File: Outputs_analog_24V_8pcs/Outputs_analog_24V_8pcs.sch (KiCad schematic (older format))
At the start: 10 parts, among them J1 Screw_Terminal_01x02, J2 Screw_Terminal_01x02, J3 Screw_Terminal_01x06, U1 74HC595

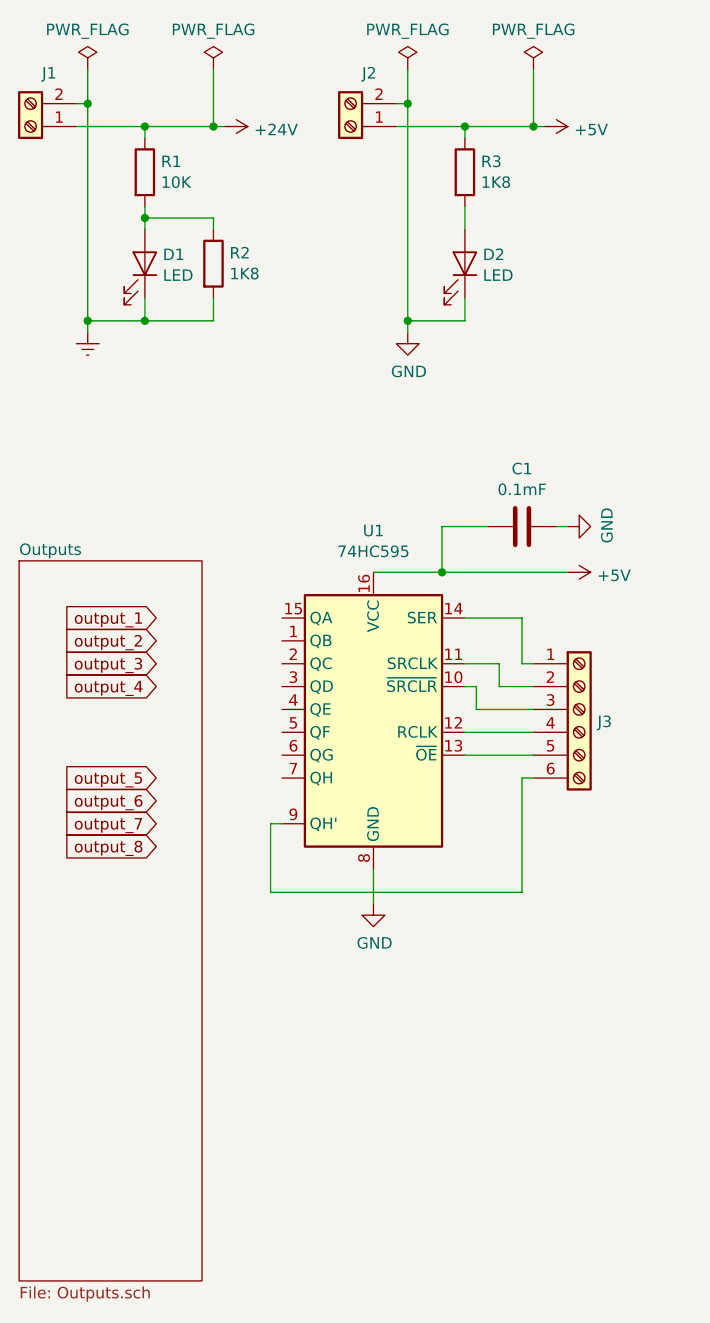
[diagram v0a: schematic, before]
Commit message: Update Outputs pcb
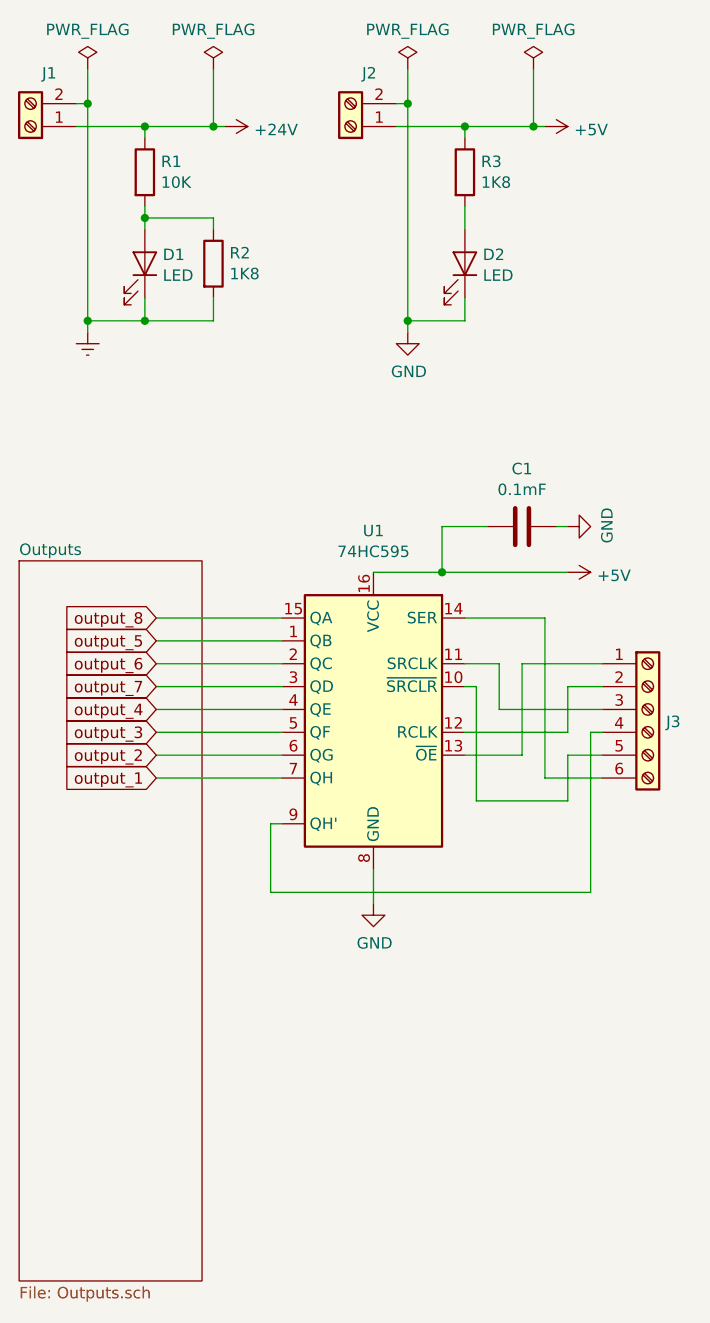
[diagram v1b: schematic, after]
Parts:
- D1, D2: footprint Diode_THT:D_A-405_P2.54mm_Vertical_AnodeUp -> LED_THT:LED_D3.0mm
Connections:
- net output_1: now also U1.7 (QH)
- net output_2: now also U1.6 (QG)
- net output_3: now also U1.5 (QF)
- net output_4: now also U1.4 (QE)
- net output_5: now also U1.1 (QB)
- net output_6: now also U1.2 (QC)
- net output_7: now also U1.3 (QD)
- net output_8: now also U1.15 (QA)
- net at J3.1 (Pin_1): now also U1.13 (~OE); no longer U1.14 (SER)
- net at J3.2 (Pin_2): now also U1.12 (RCLK); no longer U1.11 (SRCLK)
- net at J3.3 (Pin_3): now also U1.11 (SRCLK); no longer U1.10 (~SRCLR)
- net at J3.4 (Pin_4): now also U1.9 (QH'); no longer U1.12 (RCLK)
- net at J3.5 (Pin_5): now also U1.10 (~SRCLR); no longer U1.13 (~OE)
- net at J3.6 (Pin_6): now also U1.14 (SER); no longer U1.9 (QH')
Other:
- moved on the sheet: J3
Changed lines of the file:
@@
 EESchema Schematic File Version 4
-EELAYER 30 0
+LIBS:Outputs_analog_24V_8pcs-cache
+EELAYER 26 0
 EELAYER END
 $Descr A4 11693 8268
@@
 F 0 "D1" V 1589 2128 50  0000 L CNN
 F 1 "LED" V 1498 2128 50  0000 L CNN
-F 2 "Diode_THT:D_A-405_P2.54mm_Vertical_AnodeUp" H 1550 2050 50  0001 C CNN
+F 2 "LED_THT:LED_D3.0mm" H 1550 2050 50  0001 C CNN
 F 3 "~" H 1550 2050 50  0001 C CNN
 	1    1550 2050
@@
 F 0 "D2" V 2989 2128 50  0000 L CNN
 F 1 "LED" V 2898 2128 50  0000 L CNN
-F 2 "Diode_THT:D_A-405_P2.54mm_Vertical_AnodeUp" H 2950 2050 50  0001 C CNN
+F 2 "LED_THT:LED_D3.0mm" H 2950 2050 50  0001 C CNN
 F 3 "~" H 2950 2050 50  0001 C CNN
 	1    2950 2050
@@
 F1 "Outputs.sch" 50
 $EndSheet
+Text GLabel 1600 4300 0    50   Input ~ 0
+output_1
+Text GLabel 1600 4200 0    50   Input ~ 0
+output_2
+Text GLabel 1600 4100 0    50   Input ~ 0
+output_3
+Text GLabel 1600 4000 0    50   Input ~ 0
+output_4
+Text GLabel 1600 3700 0    50   Input ~ 0
+output_5
+Text GLabel 1600 3800 0    50   Input ~ 0
+output_6
+Text GLabel 1600 3900 0    50   Input ~ 0
+output_7
 Text GLabel 1600 3600 0    50   Input ~ 0
-output_1
-Text GLabel 1600 3700 0    50   Input ~ 0
-output_2
-Text GLabel 1600 3800 0    50   Input ~ 0
-output_3
-Text GLabel 1600 3900 0    50   Input ~ 0
-output_4
-Text GLabel 1600 4300 0    50   Input ~ 0
-output_5
-Text GLabel 1600 4400 0    50   Input ~ 0
-output_6
-Text GLabel 1600 4500 0    50   Input ~ 0
-output_7
-Text GLabel 1600 4600 0    50   Input ~ 0
 output_8
-$Comp
-L Connector:Screw_Terminal_01x06 J3
-U 1 1 5EADD649
-P 3450 4000
-F 0 "J3" H 3530 3946 50  0000 L CNN
-F 1 "Screw_Terminal_01x06" H 3530 3901 50  0001 L CNN
-F 2 "Connector_PinHeader_2.54mm:PinHeader_1x06_P2.54mm_Horizontal" H 3450 4000 50  0001 C CNN
-F 3 "~" H 3450 4000 50  0001 C CNN
-	1    3450 4000
-	1    0    0    -1
-$EndComp
 $Comp
 L 74xx:74HC595 U1
@@
 $EndComp
 Wire Wire Line
-	2950 3600 3200 3600
-Wire Wire Line
-	3200 3600 3200 3800
-Wire Wire Line
-	3200 3800 3250 3800
+	2150 4500 2100 4500
+Wire Wire Line
+	2100 4500 2100 4800
+Wire Wire Line
+	2550 4700 2550 4850
+Wire Wire Line
+	2850 3400 3400 3400
+Wire Wire Line
+	1600 4300 2150 4300
+Wire Wire Line
+	1600 4200 2150 4200
+Wire Wire Line
+	1600 4100 2150 4100
+Wire Wire Line
+	1600 4000 2150 4000
+Wire Wire Line
+	1600 3600 2150 3600
+Wire Wire Line
+	1600 3900 2150 3900
+Wire Wire Line
+	1600 3700 2150 3700
+Wire Wire Line
+	1600 3800 2150 3800
+$Comp
+L Connector:Screw_Terminal_01x06 J3
+U 1 1 5EADD649
+P 3750 4000
+F 0 "J3" H 3830 3946 50  0000 L CNN
+F 1 "Screw_Terminal_01x06" H 3830 3901 50  0001 L CNN
+F 2 "Connector_PinHeader_2.54mm:PinHeader_1x06_P2.54mm_Horizontal" H 3750 4000 50  0001 C CNN
+F 3 "~" H 3750 4000 50  0001 C CNN
+	1    3750 4000
+	1    0    0    -1
+$EndComp
+Wire Wire Line
+	2950 4100 3400 4100
+Wire Wire Line
+	3400 4100 3400 3900
+Wire Wire Line
+	3400 3900 3550 3900
+Wire Wire Line
+	3550 4100 3500 4100
+Wire Wire Line
+	3500 4100 3500 4800
+Wire Wire Line
+	3500 4800 2100 4800
+Wire Wire Line
+	3200 4200 3200 3800
+Wire Wire Line
+	3200 3800 3550 3800
+Wire Wire Line
+	2950 4200 3200 4200
+Wire Wire Line
+	2950 3600 3300 3600
+Wire Wire Line
+	3300 3600 3300 4300
+Wire Wire Line
+	3300 4300 3550 4300
 Wire Wire Line
 	2950 3800 3100 3800
 Wire Wire Line
-	3100 3800 3100 3900
-Wire Wire Line
-	3100 3900 3250 3900
+	3100 3800 3100 4000
+Wire Wire Line
+	3100 4000 3550 4000
 Wire Wire Line
 	2950 3900 3000 3900
 Wire Wire Line
-	3000 3900 3000 4000
-Wire Wire Line
-	3000 4000 3250 4000
-Wire Wire Line
-	2950 4100 3250 4100
-Wire Wire Line
-	2950 4200 3250 4200
-Wire Wire Line
-	2150 4500 2100 4500
-Wire Wire Line
-	2100 4500 2100 4800
-Wire Wire Line
-	2100 4800 3200 4800
-Wire Wire Line
-	3200 4800 3200 4300
-Wire Wire Line
-	3200 4300 3250 4300
-Wire Wire Line
-	2550 4700 2550 4850
-Wire Wire Line
-	2850 3400 3400 3400
+	3000 3900 3000 4400
+Wire Wire Line
+	3000 4400 3400 4400
+Wire Wire Line
+	3400 4400 3400 4200
+Wire Wire Line
+	3400 4200 3550 4200
 $EndSCHEMATC

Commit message: Update pcb
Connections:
- net output_2: now also U1.4 (QE); no longer U1.6 (QG)
- net output_4: now also U1.6 (QG); no longer U1.4 (QE)
- net output_5: now also U1.15 (QA); no longer U1.1 (QB)
- net output_6: now also U1.1 (QB); no longer U1.2 (QC)
- net output_8: now also U1.2 (QC); no longer U1.15 (QA)
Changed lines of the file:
@@
 EESchema Schematic File Version 4
-LIBS:Outputs_analog_24V_8pcs-cache
-EELAYER 26 0
+EELAYER 30 0
 EELAYER END
 $Descr A4 11693 8268
@@
 Text GLabel 1600 4300 0    50   Input ~ 0
 output_1
-Text GLabel 1600 4200 0    50   Input ~ 0
+Text GLabel 1600 4000 0    50   Input ~ 0
 output_2
 Text GLabel 1600 4100 0    50   Input ~ 0
 output_3
-Text GLabel 1600 4000 0    50   Input ~ 0
+Text GLabel 1600 4200 0    50   Input ~ 0
 output_4
+Text GLabel 1600 3600 0    50   Input ~ 0
+output_5
 Text GLabel 1600 3700 0    50   Input ~ 0
-output_5
-Text GLabel 1600 3800 0    50   Input ~ 0
 output_6
 Text GLabel 1600 3900 0    50   Input ~ 0
 output_7
-Text GLabel 1600 3600 0    50   Input ~ 0
+Text GLabel 1600 3800 0    50   Input ~ 0
 output_8
 $Comp
@@
 	1600 4300 2150 4300
 Wire Wire Line
-	1600 4200 2150 4200
-Wire Wire Line
 	1600 4100 2150 4100
-Wire Wire Line
-	1600 4000 2150 4000
-Wire Wire Line
-	1600 3600 2150 3600
-Wire Wire Line
-	1600 3900 2150 3900
-Wire Wire Line
-	1600 3700 2150 3700
 Wire Wire Line
 	1600 3800 2150 3800
@@
 Wire Wire Line
 	3400 4200 3550 4200
+Wire Wire Line
+	1600 4200 2150 4200
+Wire Wire Line
+	1600 4000 2150 4000
+Wire Wire Line
+	1600 3700 2150 3700
+Wire Wire Line
+	1600 3900 2150 3900
+Wire Wire Line
+	1600 3600 2150 3600
 $EndSCHEMATC

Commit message: Update footprints
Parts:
- J1, J2: footprint Connector_PinHeader_2.54mm:PinHeader_1x02_P2.54mm_Horizontal -> Connector_PinHeader_2.54mm:PinHeader_1x02_P2.54mm_Vertical
- J3: footprint Connector_PinHeader_2.54mm:PinHeader_1x06_P2.54mm_Horizontal -> Connector_PinHeader_2.54mm:PinHeader_1x06_P2.54mm_Vertical
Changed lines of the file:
@@
 F 0 "J1" H 968 1217 50  0000 C CNN
 F 1 "Screw_Terminal_01x02" H 1130 1351 50  0001 L CNN
-F 2 "Connector_PinHeader_2.54mm:PinHeader_1x02_P2.54mm_Horizontal" H 1050 1450 50  0001 C CNN
+F 2 "Connector_PinHeader_2.54mm:PinHeader_1x02_P2.54mm_Vertical" H 1050 1450 50  0001 C CNN
 F 3 "~" H 1050 1450 50  0001 C CNN
 	1    1050 1450
@@
 F 0 "J2" H 2368 1217 50  0000 C CNN
 F 1 "Screw_Terminal_01x02" H 2530 1351 50  0001 L CNN
-F 2 "Connector_PinHeader_2.54mm:PinHeader_1x02_P2.54mm_Horizontal" H 2450 1450 50  0001 C CNN
+F 2 "Connector_PinHeader_2.54mm:PinHeader_1x02_P2.54mm_Vertical" H 2450 1450 50  0001 C CNN
 F 3 "~" H 2450 1450 50  0001 C CNN
 	1    2450 1450
@@
 F 0 "J3" H 3830 3946 50  0000 L CNN
 F 1 "Screw_Terminal_01x06" H 3830 3901 50  0001 L CNN
-F 2 "Connector_PinHeader_2.54mm:PinHeader_1x06_P2.54mm_Horizontal" H 3750 4000 50  0001 C CNN
+F 2 "Connector_PinHeader_2.54mm:PinHeader_1x06_P2.54mm_Vertical" H 3750 4000 50  0001 C CNN
 F 3 "~" H 3750 4000 50  0001 C CNN
 	1    3750 4000
